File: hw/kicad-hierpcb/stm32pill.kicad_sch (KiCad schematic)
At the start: 12 parts, among them U2 STM32F103C8T6

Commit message: ide stm
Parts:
- removed ADC1: ADC0, base:PTH, symbol Connector:Conn_01x01_Pin
- removed AL2: Arduino Left Pins, Connector_PinHeader_2.54mm:PinHeader_1x15_P2.54mm_Vertical, symbol Connector:Conn_01x15_Pin
- removed AR2: Arduino Right Pins, Connector_PinHeader_2.54mm:PinHeader_1x15_P2.54mm_Vertical, symbol Connector:Conn_01x15_Pin
- removed Boot1: Boot0, base:PTH, symbol Connector:Conn_01x01_Pin
- removed I2C_1: I2C_2, Connector_PinHeader_2.54mm:PinHeader_1x02_P2.54mm_Vertical, symbol Connector:Conn_01x02_Pin
- removed NRST2: NRST, base:PTH, symbol Connector:Conn_01x01_Pin
- removed PC2: PC, Connector_PinHeader_2.54mm:PinHeader_1x03_P2.54mm_Vertical, symbol Connector:Conn_01x03_Pin
- removed PD2: PD, Connector_PinHeader_2.54mm:PinHeader_1x02_P2.54mm_Vertical, symbol Connector:Conn_01x02_Pin
- removed SWD2: SWD, Connector_PinHeader_2.54mm:PinHeader_1x02_P2.54mm_Vertical, symbol Connector:Conn_01x02_Pin
- removed USB2: USB, Connector_PinHeader_2.54mm:PinHeader_1x02_P2.54mm_Vertical, symbol Connector:Conn_01x02_Pin
- removed VBAT2: VBAT, base:PTH, symbol Connector:Conn_01x01_Pin
- added B0: B0 Jumper, base:3x PTH 1.7mm, symbol Connector:Conn_01x03_Socket
- added C1, C2, C3, C4: CL21B103KBANNNC, jlcpcb:C0805, symbol jlcpcb:Capacitor 10nF CL21B103KBANNNC
- added J1: IDE STM CD, ribbon:IDE STM CD, symbol ribbon:IDE STM CD
- added J2: IDE STM AB, ribbon:IDE STM AB, symbol ribbon:IDE STM AB
- renumbered U2 to U4
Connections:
- net +3.3V: now also B0.3 (Pin_3), C1.2, C2.2, C3.2, C4.2, J1.3V3 (IDE1_STM23)
- net Boot0: now also B0.2 (Pin_2)
- net GND: now also B0.1 (Pin_1), C1.1, C2.1, C3.1, C4.1, J2.GND (IDE2_STM24)
- net VBAT: now reaches U4.1 (VBAT)
- net at U4.10 (PA0-WKUP): now also J2.A4 (IDE32_STM10)
- net at U4.11 (PA1): now also J2.A3 (IDE30_STM11)
- net at U4.12 (PA2): now also J2.A2 (IDE26_STM12)
- net at U4.13 (PA3): now also J2.A1 (IDE24_STM13)
- net at U4.14 (PA4): now also J2.A0 (IDE22_STM14)
- net at U4.15 (PA5): now also J2.B7 (IDE18_STM15)
- net at U4.16 (PA6): now also J2.B6 (IDE16_STM16)
- net at U4.17 (PA7): now also J2.B5 (IDE14_STM17)
- net at U4.18 (PB0): now also J2.B4 (IDE12_STM18)
- net at U4.19 (PB1): now also J2.B3 (IDE10_STM19)
- net at U4.2 (PC13-TAMPER-RTC): now also J2.A7 (IDE40_STM2)
- net at U4.20 (PB2): now also J2.B2 (IDE8_STM20)
- net at U4.25 (PB12): now also J1.C0 (IDE5_STM25)
- net at U4.26 (PB13): now also J1.C1 (IDE7_STM26)
- net at U4.27 (PB14): now also J1.C2 (IDE9_STM27)
- net at U4.28 (PB15): now also J1.C3 (IDE11_STM28)
- net at U4.29 (PA8): now also J1.C4 (IDE13_STM29)
- net at U4.3 (PC14-OSC32_IN): now also J2.A6 (IDE38_STM3)
- net at U4.30 (PA9): now also J1.C5 (IDE15_STM30)
- net at U4.31 (PA10): now also J1.C6 (IDE17_STM31)
- net at U4.34 (PA13): now also J1.D1 (IDE23_STM34)
- net at U4.37 (PA14): now also J1.D2 (IDE25_STM37)
- net at U4.38 (PA15): now also J1.D3 (IDE27_STM38)
- net at U4.39 (PB3): now also J1.D4 (IDE29_STM39)
- net at U4.4 (PC15-OSC32_OUT): now also J2.A5 (IDE36_STM4)
- net at U4.40 (PB4): now also J1.D5 (IDE31_STM40)
- net at U4.41 (PB5): now also J1.D6 (IDE33_STM41)
- net at U4.42 (PB6): now also J1.D7 (IDE35_STM42)
- net at U4.43 (PB7): now also J1.VBusSense (IDE3_STM43)
- net at U4.45 (PB8): now also J1.SCL (IDE37_STM45)
- net at U4.46 (PB9): now also J1.SDA (IDE39_STM46)
- net OSC_IN: now reaches U4.5 (PD0-OSC_IN)
- net OSC_OUT: now reaches U4.6 (PD1-OSC_OUT)
- net NRST: now reaches U4.7 (NRST)
- net SCL: no longer names the net of U4.21 (PB10)
- net SCL: now also J2.B1 (IDE6_STM21)
- net SDA: no longer names the net of U4.22 (PB11)
- net SDA: now also J2.B0 (IDE4_STM22)
- net USBD+: no longer names the net of U4.33 (PA12)
- net USBD+: now also J1.D0 (IDE21_STM33)
- net USBD-: no longer names the net of U4.32 (PA11)
- net USBD-: now also J1.C7 (IDE19_STM32)

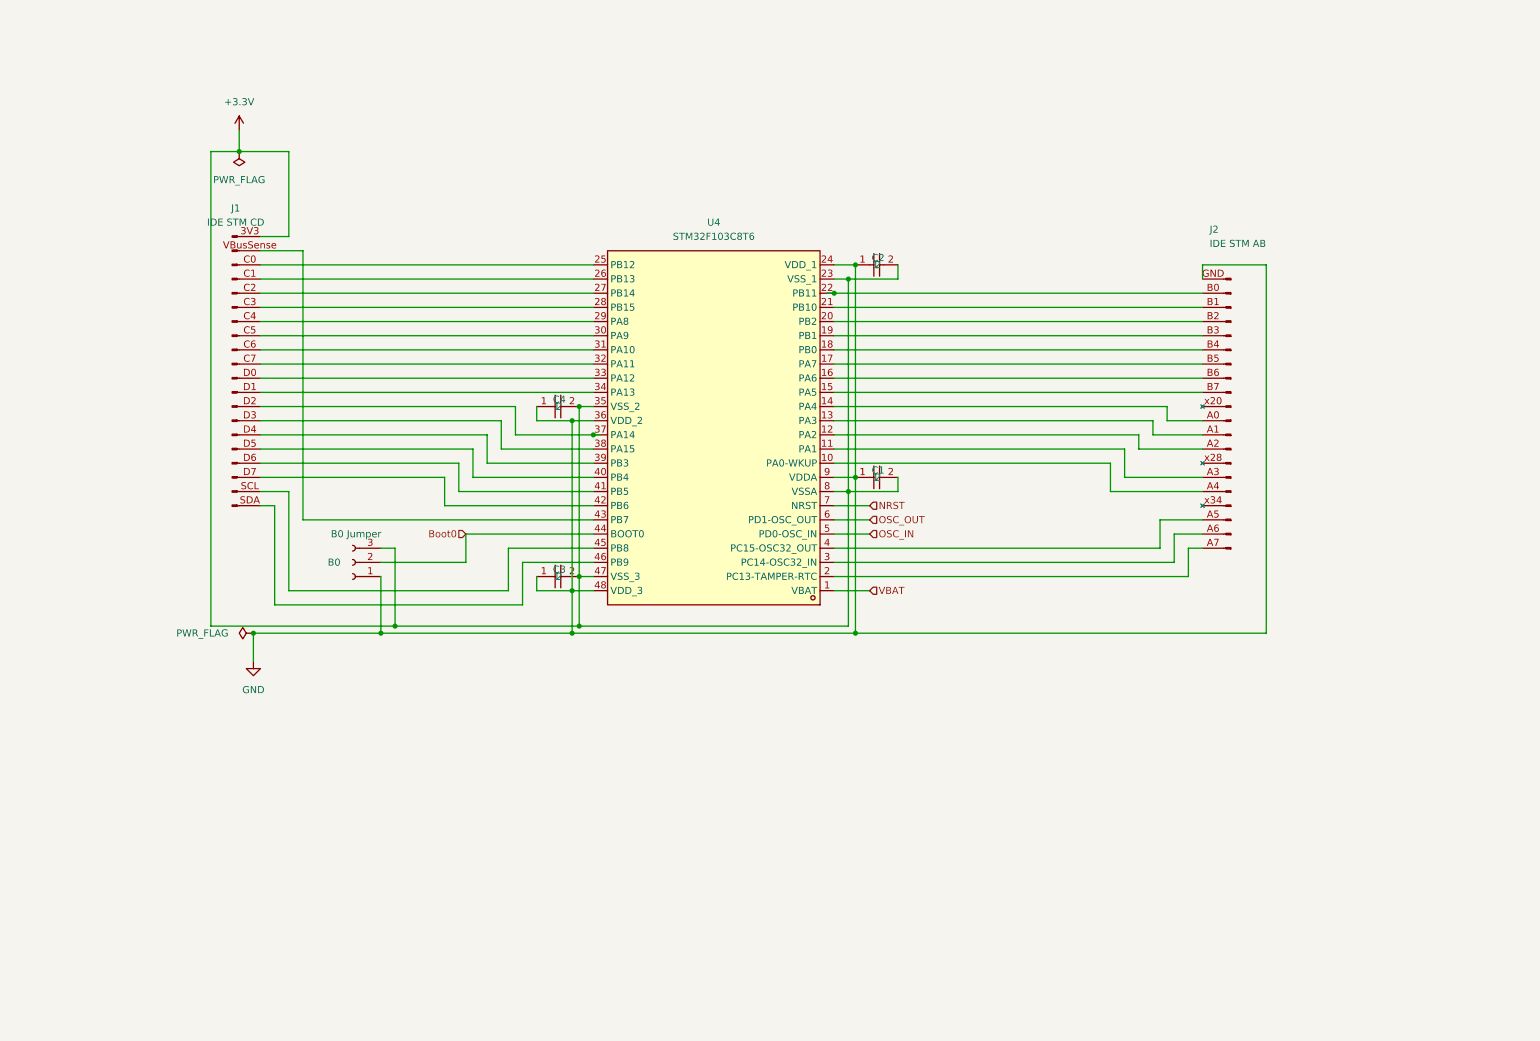
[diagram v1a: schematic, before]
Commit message: stm32pill pcb
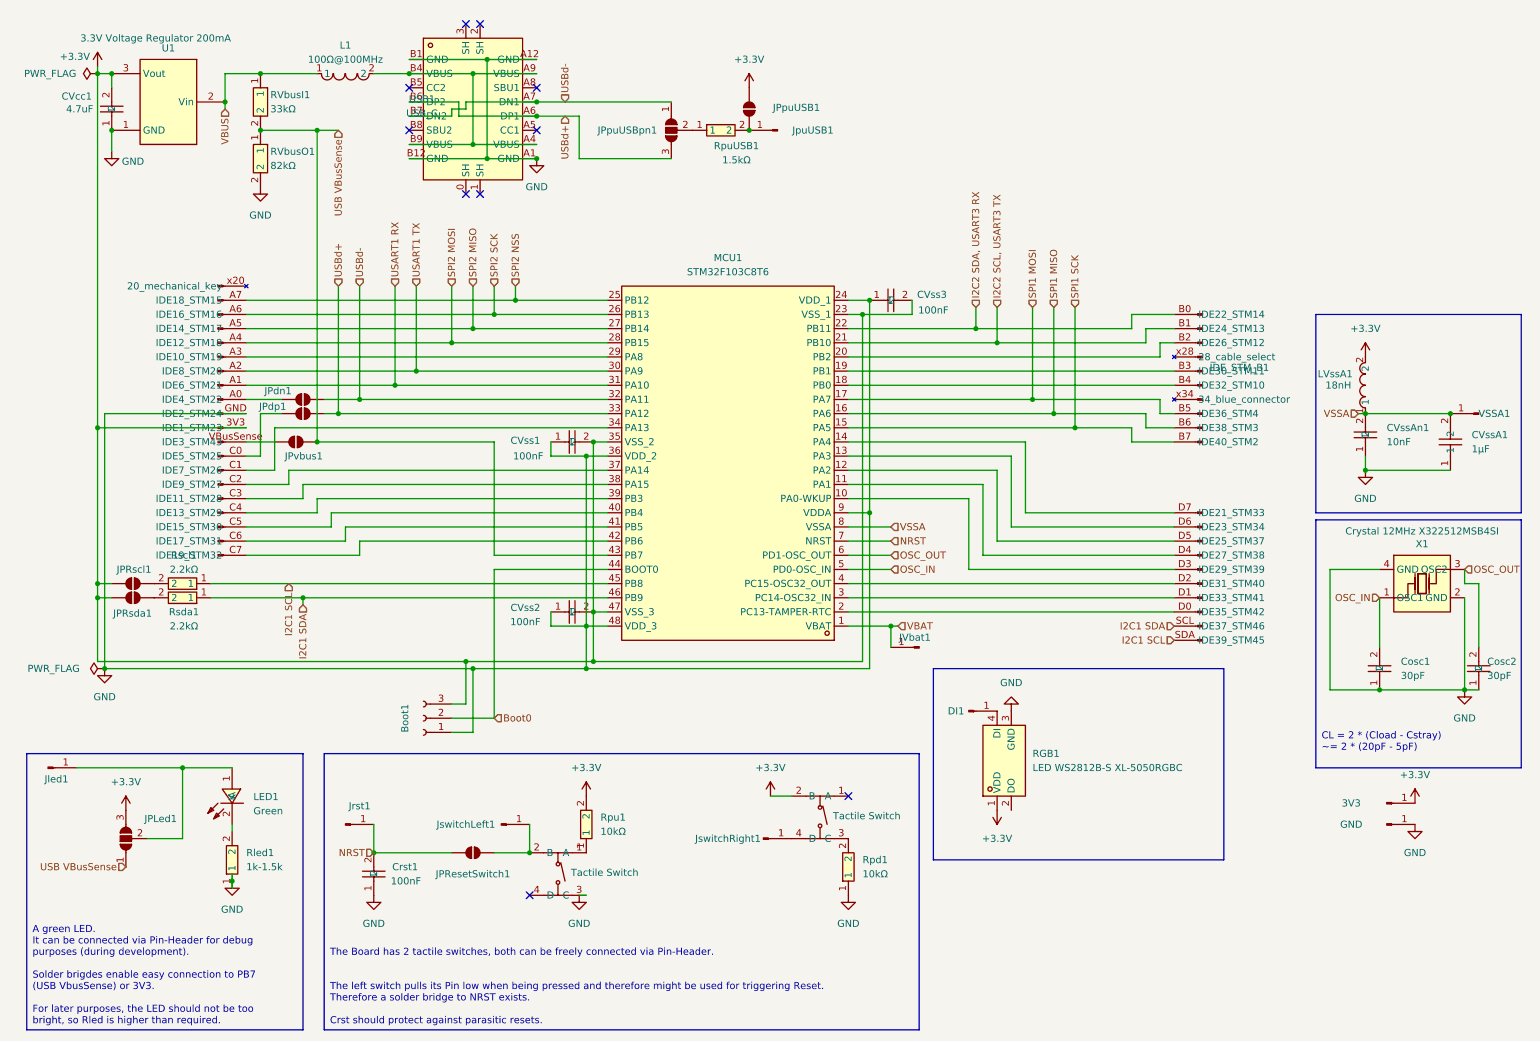
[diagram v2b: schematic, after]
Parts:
- removed C1: CL21B103KBANNNC, jlcpcb:C0805, symbol jlcpcb:Capacitor 10nF CL21B103KBANNNC
- removed J1: IDE STM CD, ribbon:IDE STM CD, symbol ribbon:IDE STM CD
- removed J2: IDE STM AB, ribbon:IDE STM AB, symbol ribbon:IDE STM AB
- added 3V3, DI1, GND, Jled1, JpuUSB1, Jrst1, JswitchLeft1, JswitchRight1: ~, base:PTH 1.7mm, symbol Connector:Conn_01x01_Pin
- added CVcc1: 4.7uF, jlcpcb:C1206, symbol jlcpcb:Capacitor 4.7uF 1206B475K500NT
- added CVssA1: 1μF, jlcpcb:C0402, symbol jlcpcb:Capacitor 1μF 0402 CL05A105KA5NQNC
- added CVssAn1: 10nF, jlcpcb:C0402, symbol jlcpcb:Capacitor 10nF 0402 CL05B103KB5NNNC
- added Cosc1, Cosc2: 30pF, jlcpcb:C0402, symbol jlcpcb:Capacitor 30pF 0402CG300J500NT
- added Crst1: 100nF, jlcpcb:C0402, symbol jlcpcb:Capacitor 100nF 0402F104M500NT
- added IDE_STM_A1: ~, ribbon:IDE STM A, symbol ribbon:IDE_STM_A
- added IDE_STM_B1: ~, ribbon:IDE STM B, symbol ribbon:IDE_STM_B
- added IDE_STM_C1: ~, ribbon:IDE STM C, symbol ribbon:IDE_STM_C
- added IDE_STM_D1: ~, ribbon:IDE STM D, symbol ribbon:IDE_STM_D
- added JPLed1, JPpuUSBpn1: SolderJumper_3_Open, Jumper:SolderJumper-3_P1.3mm_Open_RoundedPad1.0x1.5mm, symbol Jumper:SolderJumper_3_Open
- added JPResetSwitch1, JPRscl1, JPRsda1, JPdn1, JPdp1, JPpuUSB1, JPvbus1: SolderJumper_2_Open, Jumper:SolderJumper-2_P1.3mm_Open_RoundedPad1.0x1.5mm, symbol Jumper:SolderJumper_2_Open
- added JVbat1: VBAT, TestPoint:TestPoint_THTPad_D1.0mm_Drill0.5mm, symbol Connector:Conn_01x01_Pin
- added L1: 100Ω@100MHz, jlcpcb:L0805, symbol jlcpcb:Ferrite Beads 100Ω@100MHz GZ2012D101TF
- added LED1: Green, jlcpcb:LED0805-R-RD, symbol jlcpcb:LED green 0805G(Green)
- added LVssA1: 18nH, jlcpcb:L0201, symbol jlcpcb:Inductor 18nH CHQ0603T-18NH-HU
- added RGB1: LED WS2812B-S XL-5050RGBC, jlcpcb:LED-SMD_4P-L5.0-W5.0-TL-1, symbol jlcpcb:LED WS2812B-S XL-5050RGBC
- added RVbusI1: 33kΩ, jlcpcb:R0402, symbol jlcpcb:Resistor 33kΩ 0402 SCR0402J33K
- added RVbusO1: 82kΩ, jlcpcb:R0402, symbol jlcpcb:Resistor 82kΩ 0402 SCR0402J82K
- added Rled1: 1k-1.5k, jlcpcb:R0402, symbol jlcpcb:Resistor 1kΩ 0402WGF1001TCE
- added Rpd1, Rpu1: 10kΩ, jlcpcb:R0402, symbol jlcpcb:Resistor 10kΩ 0402WGF1002TCE
- added RpuUSB1: 1.5kΩ, jlcpcb:R0402, symbol jlcpcb:Resistor 1.5kΩ 0402WGF1501TCE
- added Rscl1, Rsda1: 2.2kΩ, jlcpcb:R0402, symbol jlcpcb:Resistor 2.2kΩ 0402WGF2201TCE
- added SW1, SW2: Tactile Switch, jlcpcb:SW-SMD_4P-L5.1-W5.1-P3.70-LS6.5-TL_H1.5, symbol jlcpcb:Tactile Switch TS-1187A-B-A-B
- added U1: 3.3V Voltage Regulator 200mA, jlcpcb:SOT-23-3_L2.9-W1.6-P1.90-LS2.8-BR, symbol jlcpcb:3.3V Voltage Regulator 200mA XC6206P332MR
- added USB1: USB_C, jlcpcb:USB-C_SMD-TYPE-C-31-M-12, symbol jlcpcb:USB C female horizontal 16pin DEALON 018
- added VSSA1: VSSA, TestPoint:TestPoint_THTPad_D1.0mm_Drill0.5mm, symbol Connector:Conn_01x01_Pin
- added X1: Crystal 12MHz X322512MSB4SI, jlcpcb:CRYSTAL-SMD_4P-L3.2-W2.5-BL, symbol jlcpcb:Crystal 12MHz X322512MSB4SI
- Boot1: renamed from B0; value B0 Jumper -> ~
- CVss1: renamed from C4; value CL21B103KBANNNC -> 100nF; footprint jlcpcb:C0805 -> jlcpcb:C0402; symbol jlcpcb:Capacitor 10nF CL21B103KBANNNC -> jlcpcb:Capacitor 100nF 0402F104M500NT; LCSC Part C1710 -> C1581
- CVss2: renamed from C3; value CL21B103KBANNNC -> 100nF; footprint jlcpcb:C0805 -> jlcpcb:C0402; symbol jlcpcb:Capacitor 10nF CL21B103KBANNNC -> jlcpcb:Capacitor 100nF 0402F104M500NT; LCSC Part C1710 -> C1581
- CVss3: renamed from C2; value CL21B103KBANNNC -> 100nF; footprint jlcpcb:C0805 -> jlcpcb:C0402; symbol jlcpcb:Capacitor 10nF CL21B103KBANNNC -> jlcpcb:Capacitor 100nF 0402F104M500NT; LCSC Part C1710 -> C1581
- renumbered U4 to MCU1
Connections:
- net +3.3V: now also 3V3.1 (Pin_1), CVcc1.2, IDE_STM_C1.3V3 (IDE1_STM23), JPLed1.3 (B), JPRscl1.2 (B), JPRsda1.1 (A), JPpuUSB1.2 (B), LVssA1.2, RGB1.1 (VDD), Rpu1.2, SW2.2 (B), U1.3 (Vout); no longer MCU1.8 (VSSA)
- net GND: now also CVcc1.1, CVssA1.1, CVssAn1.1, Cosc1.1, Cosc2.1, Crst1.1, GND.1 (Pin_1), IDE_STM_A1.GND (IDE2_STM24), RGB1.3 (GND), RVbusO1.2, Rled1.1, Rpd1.1, SW1.3 (C), U1.1 (GND), USB1.A1 (GND), USB1.A12 (GND), USB1.B1 (GND), USB1.B12 (GND), X1.2 (GND), X1.4 (GND)
- net NRST: now also Crst1.2, JPResetSwitch1.1 (A), Jrst1.1 (Pin_1)
- net OSC_IN: now also Cosc1.2, X1.1 (OSC1)
- net OSC_OUT: now also Cosc2.2, X1.3 (OSC2)
- net VBAT: now also JVbat1.1 (Pin_1)
- net at MCU1.10 (PA0-WKUP): now also IDE_STM_D1.D3 (IDE29_STM39)
- net at MCU1.11 (PA1): now also IDE_STM_D1.D4 (IDE27_STM38)
- net at MCU1.12 (PA2): now also IDE_STM_D1.D5 (IDE25_STM37)
- net at MCU1.13 (PA3): now also IDE_STM_D1.D6 (IDE23_STM34)
- net at MCU1.14 (PA4): now also IDE_STM_D1.D7 (IDE21_STM33)
- net SPI1 SCK: now reaches MCU1.15 (PA5)
- net SPI1 SCK: now also IDE_STM_B1.B7 (IDE40_STM2)
- net SPI1 MISO: now reaches MCU1.16 (PA6)
- net SPI1 MISO: now also IDE_STM_B1.B6 (IDE38_STM3)
- net SPI1 MOSI: now reaches MCU1.17 (PA7)
- net SPI1 MOSI: now also IDE_STM_B1.B5 (IDE36_STM4)
- net at MCU1.18 (PB0): now also IDE_STM_B1.B4 (IDE32_STM10)
- net at MCU1.19 (PB1): now also IDE_STM_B1.B3 (IDE30_STM11)
- net at MCU1.2 (PC13-TAMPER-RTC): now also IDE_STM_D1.D0 (IDE35_STM42)
- net at MCU1.20 (PB2): now also IDE_STM_B1.B2 (IDE26_STM12)
- net I2C2 SCL, USART3 TX: now reaches MCU1.21 (PB10)
- net I2C2 SCL, USART3 TX: now also IDE_STM_B1.B1 (IDE24_STM13)
- net I2C2 SDA, USART3 RX: now reaches MCU1.22 (PB11)
- net I2C2 SDA, USART3 RX: now also IDE_STM_B1.B0 (IDE22_STM14)
- net SPI2 NSS: now reaches MCU1.25 (PB12)
- net SPI2 NSS: now also IDE_STM_A1.A7 (IDE18_STM15)
- net SPI2 SCK: now reaches MCU1.26 (PB13)
- net SPI2 SCK: now also IDE_STM_A1.A6 (IDE16_STM16)
- net SPI2 MISO: now reaches MCU1.27 (PB14)
- net SPI2 MISO: now also IDE_STM_A1.A5 (IDE14_STM17)
- net SPI2 MOSI: now reaches MCU1.28 (PB15)
- net SPI2 MOSI: now also IDE_STM_A1.A4 (IDE12_STM18)
- net at MCU1.29 (PA8): now also IDE_STM_A1.A3 (IDE10_STM19)
- net at MCU1.3 (PC14-OSC32_IN): now also IDE_STM_D1.D1 (IDE33_STM41)
- net USART1 TX: now reaches MCU1.30 (PA9)
- net USART1 TX: now also IDE_STM_A1.A2 (IDE8_STM20)
- net USART1 RX: now reaches MCU1.31 (PA10)
- net USART1 RX: now also IDE_STM_A1.A1 (IDE6_STM21)
- net USBd-: now reaches MCU1.32 (PA11)
- net USBd-: now also JPdn1.1 (A), JPpuUSBpn1.1 (A), USB1.A7 (DN1), USB1.B7 (DN2)
- net USBd+: now reaches MCU1.33 (PA12)
- net USBd+: now also JPdp1.2 (B), JPpuUSBpn1.3 (B), USB1.A6 (DP1), USB1.B6 (DP2)
- net at MCU1.34 (PA13): now also IDE_STM_C1.C1 (IDE7_STM26)
- net at MCU1.37 (PA14): now also IDE_STM_C1.C2 (IDE9_STM27)
- net at MCU1.38 (PA15): now also IDE_STM_C1.C3 (IDE11_STM28)
- net at MCU1.39 (PB3): now also IDE_STM_C1.C4 (IDE13_STM29)
- net at MCU1.4 (PC15-OSC32_OUT): now also IDE_STM_D1.D2 (IDE31_STM40)
- net at MCU1.40 (PB4): now also IDE_STM_C1.C5 (IDE15_STM30)
- net at MCU1.41 (PB5): now also IDE_STM_C1.C6 (IDE17_STM31)
- net at MCU1.42 (PB6): now also IDE_STM_C1.C7 (IDE19_STM32)
- net USB VBusSense: now reaches MCU1.43 (PB7)
- net USB VBusSense: now also JPLed1.1 (A), JPvbus1.1 (A), RVbusI1.2, RVbusO1.1
- net I2C1 SCL: now reaches MCU1.45 (PB8)
- net I2C1 SCL: now also IDE_STM_D1.SDA (IDE39_STM45), Rscl1.1
- net I2C1 SDA: now reaches MCU1.46 (PB9)
- net I2C1 SDA: now also IDE_STM_D1.SCL (IDE37_STM46), Rsda1.1
- new net: Rpd1.2, SW2.3 (C)
- new net: IDE_STM_A1.A0 (IDE4_STM22), JPdn1.2 (B)
- new net: L1.2, USB1.A4 (VBUS), USB1.A9 (VBUS), USB1.B4 (VBUS), USB1.B9 (VBUS)
- new net: IDE_STM_C1.C0 (IDE5_STM25), JPdp1.1 (A)
- new net: IDE_STM_C1.VBusSense (IDE3_STM43), JPvbus1.2 (B)
- new net: JswitchRight1.1 (Pin_1), SW2.4 (D)
- new net: JPResetSwitch1.2 (B), JswitchLeft1.1 (Pin_1), SW1.2 (B)
- new net: JPRscl1.1 (A), Rscl1.2
- new net: JPpuUSB1.1 (A), JpuUSB1.1 (Pin_1), RpuUSB1.2
- new net: Rpu1.1, SW1.1 (A)
- new net: JPRsda1.2 (B), Rsda1.2
- new net: DI1.1 (Pin_1), RGB1.4 (DI)
- new net: JPLed1.2 (C), Jled1.1 (Pin_1), LED1.1 (A)
- new net: LED1.2 (K), Rled1.2
- new net: JPpuUSBpn1.2 (C), RpuUSB1.1
- new net VBUS: L1.1, RVbusI1.1, U1.2 (Vin)
- new net VSSA: CVssA1.2, CVssAn1.2, LVssA1.1, MCU1.8 (VSSA), VSSA1.1 (Pin_1)
- no-connect marks 0 -> 10
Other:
- moved on the sheet: Boot1, CVss1, CVss2, CVss3, MCU1

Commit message: stm32-panel
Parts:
- removed 3V3, GND: ~, base:PTH 1.7mm, symbol Connector:Conn_01x01_Pin
- added 3.3V1, GND1: ~, base:PTH 1.7mm, symbol Connector:Conn_01x01_Pin
- added JPV1: SolderJumper_2_Open, Jumper:SolderJumper-2_P1.3mm_Open_RoundedPad1.0x1.5mm, symbol Jumper:SolderJumper_2_Open
- added RpuBoot1: 33kΩ, jlcpcb:R0402, symbol jlcpcb:Resistor 33kΩ 0402 SCR0402J33K
- renumbered JPResetSwitch1 to JPReset1, JPpuUSBpn1 to JPpuUSB1, JPpuUSB1 to JPpuUSBconst1, JswitchRight1 to JSH1, JswitchLeft1 to JSL1
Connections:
- net +3.3V: now also 3.3V1.1 (Pin_1), JPV1.2 (B), RpuBoot1.1; no longer IDE_STM_C1.3V3 (IDE1_STM23)
- net Boot0: now also RpuBoot1.2
- net GND: now also GND1.1 (Pin_1)
- new net: IDE_STM_C1.3V3 (IDE1_STM23), JPV1.1 (A)
- no-connect marks 10 -> 11
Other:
- moved on the sheet: Boot1

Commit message: bus
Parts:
- CVss1, CVss2, CVss3, Crst1: symbol jlcpcb:Capacitor 100nF 0402F104M500NT -> jlcpcb:Capacitor 100nF 4002 CL05B104KO5NNNC; LCSC Part C1581 -> C1525
- IDE_STM_B1: footprint ribbon:IDE STM B -> ribbon:IDE STM B cut
- IDE_STM_D1: footprint ribbon:IDE STM D -> ribbon:IDE STM D cut
- LVssA1: value 18nH -> 15-30nH; footprint jlcpcb:L0201 -> jlcpcb:L0402; symbol jlcpcb:Inductor 18nH CHQ0603T-18NH-HU -> jlcpcb:Inductor 15nH SDCL1005C15NJTDF; LCSC Part C2913989 -> C27143
- RVbusI1, RpuBoot1: value 33kΩ -> 51kΩ; symbol jlcpcb:Resistor 33kΩ 0402 SCR0402J33K -> jlcpcb:Resistor 51kΩ 0402WGF5102TCE; LCSC Part C3017504 -> C25794
- RVbusO1: value 82kΩ -> 100kΩ; symbol jlcpcb:Resistor 82kΩ 0402 SCR0402J82K -> jlcpcb:Resistor 100kΩ 0402WGF1003TCE; LCSC Part C3017512 -> C25741
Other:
- moved on the sheet: CVss1, CVss2, CVss3, Crst1
